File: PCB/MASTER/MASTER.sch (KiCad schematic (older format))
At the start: 13 parts, among them J1 Conn_01x02, J2 Conn_01x03, U1 NRF24L01_Breakout, U2 LM2596-Breakout-Board

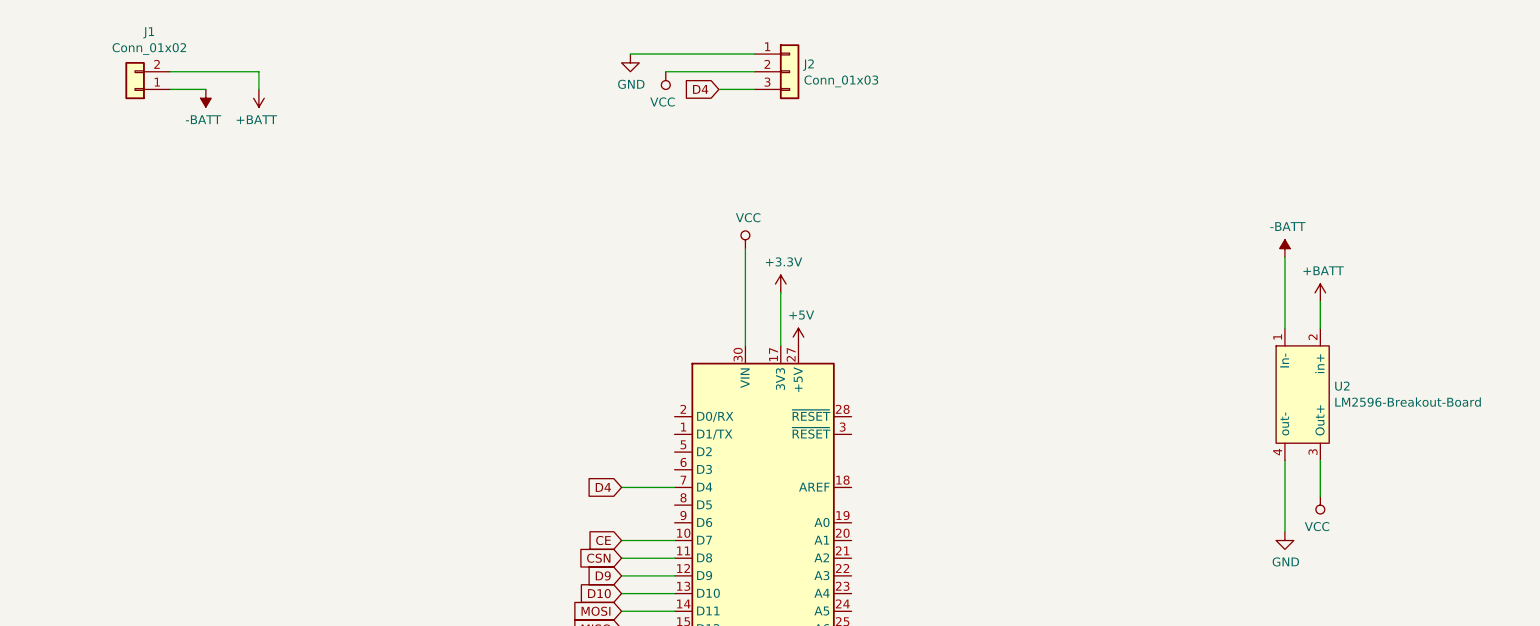
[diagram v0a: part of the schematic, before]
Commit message: Completed approximate layout. Need to route
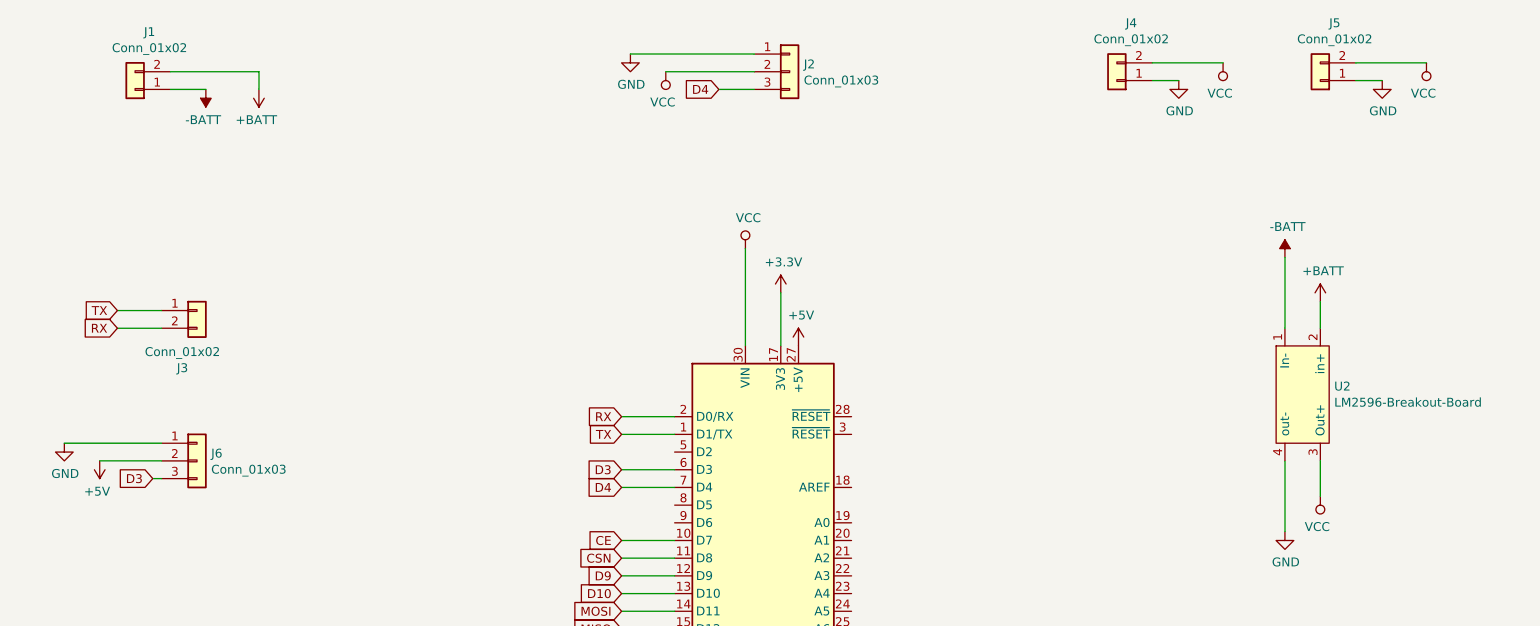
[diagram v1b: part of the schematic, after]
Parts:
- added J3: Conn_01x02, Connector_PinHeader_2.54mm:PinHeader_1x02_P2.54mm_Vertical, symbol Connector_Generic:Conn_01x02
- added J4, J5: Conn_01x02, Connector_Molex:Molex_Micro-Fit_3.0_43650-0200_1x02_P3.00mm_Horizontal, symbol Connector_Generic:Conn_01x02
- added J6: Conn_01x03, Connector_PinHeader_2.54mm:PinHeader_1x03_P2.54mm_Vertical, symbol Connector_Generic:Conn_01x03
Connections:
- net +5V: now also J6.2 (Pin_2)
- net GND: now also J4.1 (Pin_1), J5.1 (Pin_1), J6.1 (Pin_1)
- net VCC: now also J4.2 (Pin_2), J5.2 (Pin_2)
- net TX: now reaches A1.1 (D1/TX)
- net TX: now also J3.1 (Pin_1)
- net RX: now reaches A1.2 (D0/RX)
- net RX: now also J3.2 (Pin_2)
- net D3: now reaches A1.6 (D3)
- net D3: now also J6.3 (Pin_3)
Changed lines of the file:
@@
 	-1   0    0    1
 $EndComp
+Text GLabel 4000 2950 0    50   Input ~ 0
+RX
+Text GLabel 4000 3050 0    50   Input ~ 0
+TX
+Wire Wire Line
+	4000 3050 4300 3050
+Wire Wire Line
+	4000 2950 4300 2950
+Text GLabel 1150 2450 0    50   Input ~ 0
+RX
+Text GLabel 1150 2350 0    50   Input ~ 0
+TX
+$Comp
+L Connector_Generic:Conn_01x02 J4
+U 1 1 5EB3F66F
+P 6800 1050
+F 0 "J4" H 6718 725 50  0000 C CNN
+F 1 "Conn_01x02" H 6718 816 50  0000 C CNN
+F 2 "Connector_Molex:Molex_Micro-Fit_3.0_43650-0200_1x02_P3.00mm_Horizontal" H 6800 1050 50  0001 C CNN
+F 3 "~" H 6800 1050 50  0001 C CNN
+	1    6800 1050
+	-1   0    0    1
+$EndComp
+$Comp
+L power:GND #PWR0122
+U 1 1 5EB40110
+P 7150 1050
+F 0 "#PWR0122" H 7150 800 50  0001 C CNN
+F 1 "GND" H 7155 877 50  0000 C CNN
+F 2 "" H 7150 1050 50  0001 C CNN
+F 3 "" H 7150 1050 50  0001 C CNN
+	1    7150 1050
+	1    0    0    -1
+$EndComp
+$Comp
+L power:VCC #PWR0123
+U 1 1 5EB40E7C
+P 7400 950
+F 0 "#PWR0123" H 7400 800 50  0001 C CNN
+F 1 "VCC" H 7417 1123 50  0000 C CNN
+F 2 "" H 7400 950 50  0001 C CNN
+F 3 "" H 7400 950 50  0001 C CNN
+	1    7400 950
+	-1   0    0    1
+$EndComp
+Wire Wire Line
+	7000 950  7400 950
+Wire Wire Line
+	7000 1050 7150 1050
+$Comp
+L Connector_Generic:Conn_01x02 J3
+U 1 1 5EB45651
+P 1600 2350
+F 0 "J3" H 1518 2025 50  0000 C CNN
+F 1 "Conn_01x02" H 1518 2116 50  0000 C CNN
+F 2 "Connector_PinHeader_2.54mm:PinHeader_1x02_P2.54mm_Vertical" H 1600 2350 50  0001 C CNN
+F 3 "~" H 1600 2350 50  0001 C CNN
+	1    1600 2350
+	1    0    0    -1
+$EndComp
+Wire Wire Line
+	1150 2450 1400 2450
+Wire Wire Line
+	1400 2350 1150 2350
+$Comp
+L Connector_Generic:Conn_01x02 J5
+U 1 1 5EB56929
+P 7950 1050
+F 0 "J5" H 7868 725 50  0000 C CNN
+F 1 "Conn_01x02" H 7868 816 50  0000 C CNN
+F 2 "Connector_Molex:Molex_Micro-Fit_3.0_43650-0200_1x02_P3.00mm_Horizontal" H 7950 1050 50  0001 C CNN
+F 3 "~" H 7950 1050 50  0001 C CNN
+	1    7950 1050
+	-1   0    0    1
+$EndComp
+$Comp
+L power:GND #PWR0124
+U 1 1 5EB5692F
+P 8300 1050
+F 0 "#PWR0124" H 8300 800 50  0001 C CNN
+F 1 "GND" H 8305 877 50  0000 C CNN
+F 2 "" H 8300 1050 50  0001 C CNN
+F 3 "" H 8300 1050 50  0001 C CNN
+	1    8300 1050
+	1    0    0    -1
+$EndComp
+$Comp
+L power:VCC #PWR0125
+U 1 1 5EB56935
+P 8550 950
+F 0 "#PWR0125" H 8550 800 50  0001 C CNN
+F 1 "VCC" H 8567 1123 50  0000 C CNN
+F 2 "" H 8550 950 50  0001 C CNN
+F 3 "" H 8550 950 50  0001 C CNN
+	1    8550 950
+	-1   0    0    1
+$EndComp
+Wire Wire Line
+	8150 950  8550 950
+Wire Wire Line
+	8150 1050 8300 1050
+$Comp
+L Connector_Generic:Conn_01x03 J6
+U 1 1 5EB7503F
+P 1600 3200
+F 0 "J6" H 1680 3242 50  0000 L CNN
+F 1 "Conn_01x03" H 1680 3151 50  0000 L CNN
+F 2 "Connector_PinHeader_2.54mm:PinHeader_1x03_P2.54mm_Vertical" H 1600 3200 50  0001 C CNN
+F 3 "~" H 1600 3200 50  0001 C CNN
+	1    1600 3200
+	1    0    0    -1
+$EndComp
+$Comp
+L power:GND #PWR0126
+U 1 1 5EB76185
+P 850 3100
+F 0 "#PWR0126" H 850 2850 50  0001 C CNN
+F 1 "GND" H 855 2927 50  0000 C CNN
+F 2 "" H 850 3100 50  0001 C CNN
+F 3 "" H 850 3100 50  0001 C CNN
+	1    850  3100
+	1    0    0    -1
+$EndComp
+$Comp
+L power:+5V #PWR0127
+U 1 1 5EB76D83
+P 1050 3200
+F 0 "#PWR0127" H 1050 3050 50  0001 C CNN
+F 1 "+5V" H 1065 3373 50  0000 C CNN
+F 2 "" H 1050 3200 50  0001 C CNN
+F 3 "" H 1050 3200 50  0001 C CNN
+	1    1050 3200
+	-1   0    0    1
+$EndComp
+Text GLabel 4000 3250 0    50   Input ~ 0
+D3
+Wire Wire Line
+	4000 3250 4300 3250
+Text GLabel 1350 3300 0    50   Input ~ 0
+D3
+Wire Wire Line
+	1400 3200 1050 3200
+Wire Wire Line
+	850  3100 1400 3100
+Wire Wire Line
+	1400 3300 1350 3300
 $EndSCHEMATC

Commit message: routed board
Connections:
- net D10: now also R1.2; no longer R2.2
- net D9: now also R2.2; no longer R1.2
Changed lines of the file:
@@
 	1    0    0    -1
 $EndComp
+Text GLabel 850  7550 0    50   Input ~ 0
+D9
 Text GLabel 850  6900 0    50   Input ~ 0
-D9
-Text GLabel 850  7550 0    50   Input ~ 0
 D10
 Text GLabel 4000 3850 0    50   Input ~ 0

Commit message: All schematics detail check complete
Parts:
- D1: value LED -> R-LED; Field4 (none) -> 160-1447-1-ND
- D2: value LED -> G-LED; Field4 (none) -> 160-1443-6-ND
- R1, R2: value R -> 220 ohm; Field4 (none) -> P220BZCT-ND
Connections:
- net D10: now also R2.2; no longer R1.2
- net D9: now also R1.2; no longer R2.2
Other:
- note added: "Buck Regulator"
- note added: "Future Auxiliary Ports"
- note added: "Indicators"
- note added: "Microcontroller"
- note added: "Mounting"
- note added: "Power In"
- note added: "Power Out"
- note added: "RF Communication"
- note added: "Servo"
- moved on the sheet: A1, J1, J2, J3, J4, J5, J6, U1, U2
